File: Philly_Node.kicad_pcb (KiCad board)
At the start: 2 copper layers, 22 x 38.8 mm, 50 parts, among them J4 USB_C_Receptacle_USB2.0, J5 J-Link, Q4 Q_NMOS_GSD, U1 MDBT50Q-U1MV2, U2 BQ25101, U7 E22-900M22S, Y1 32.768KHz

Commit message: Nearly done, final part number checks needed.
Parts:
- removed D6, D7, D8: LESD5D5_0CT1G, pager_parts:SOD-523_L1.2-W0.8-LS1.6-BI
- added C7: 100uf, Capacitor_SMD:CP_Elec_5x4.5, B.Cu at (97.7, 50.0)
- added F1: Polyfuse 3.5A, Fuse:Fuse_1206_3216Metric, F.Cu at (99.0, 58.6)
- added J1: LED, Connector_PinSocket_1.00mm:PinSocket_1x03_P1.00mm_Vertical, F.Cu at (98.4, 75.7)
- added Q1: Q_Dual_NMOS_G1S2G2D2S1D1, Library:DFN-6-1EP_2x2mm_P0.65mm_EP_DUAL, B.Cu at (81.9, 76.5)
- added R22: 22, Resistor_SMD:R_0402_1005Metric, B.Cu at (87.2, 77.2)
- added R23: 1M, Resistor_SMD:R_0402_1005Metric, B.Cu at (85.2, 77.2)
- added R24: 22, Resistor_SMD:R_0402_1005Metric, B.Cu at (87.2, 76.2)
- added R25: 1M, Resistor_SMD:R_0402_1005Metric, B.Cu at (85.2, 76.2)
- added SOL1: S2B-PH-SM4-TB, Connector_JST:JST_PH_S2B-PH-SM4-TB_1x02-1MP_P2.00mm_Horizontal, F.Cu at (85.8, 50.0)
- D1, D2: value 1N5819WS -> B5819WT; footprint Diode_SMD:D_SOD-323 -> Diode_SMD:D_SOD-523
- J5: value J-Link -> Multi
- moved D3 4.70 mm to (99.3, 62.7)
- moved D2 3.17 mm to (90.2, 46.6), turned to 90 degrees
- moved R11 2.29 mm to (100.8, 76.2), turned to -90 degrees
- moved R16 2.13 mm to (97.8, 64.4)
- moved R6 1.43 mm to (90.9, 54.6)
- moved LED1 1.40 mm to (98.3, 79.0)
- moved R10 1.19 mm to (99.8, 76.2), turned to -90 degrees
- moved D1 1.14 mm to (90.8, 53.1)
- moved R5 0.92 mm to (85.7, 55.5)
- moved D5 0.66 mm to (81.2, 56.3)
- moved D4 0.63 mm to (82.7, 56.3)
- moved BAT1 0.62 mm to (96.6, 51.2)
- moved Q4 0.30 mm to (99.4, 66.2), turned to 180 degrees
- renumbered BT1 to BAT1
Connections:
- BAT1 pad 1: /VBAT -> /VBAT_UNFUSED
- C30 pad 1: /VBAT -> /VBAT_UNFUSED
- D3 pad 2: /VBAT -> /VBAT_FUSED
- J5 pad 10: unconnected-(J5-Pin_10-Pad10) -> NMOS_2
- J5 pad 5: GND -> P1.12_RX
- J5 pad 6: unconnected-(J5-Pin_6-Pad6) -> P1.11_TX
- J5 pad 7: unconnected-(J5-Pin_7-Pad7) -> GND
- J5 pad 8: unconnected-(J5-Pin_8-Pad8) -> VBAT_POL_PROT
- J5 pad 9: GND -> NMOS_1
- R8 pad 1: /VBAT -> /VBAT_UNFUSED
- U1 pad 4: unconnected-(U1-P1.11-Pad4) -> P1.11_TX
- U1 pad 42: unconnected-(U1-P0.19-Pad42) -> P0.19
- U1 pad 44: unconnected-(U1-P0.20-Pad44) -> P0.20
- U1 pad 5: unconnected-(U1-P1.12-Pad5) -> P1.12_RX
- U2 pad A1: /VBAT -> /VBAT_UNFUSED
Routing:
- net /VBAT_UNFUSED: track 0.00 -> 39.9 mm, vias 0 -> 2
- net /VBAT: track 36.1 -> 0.00 mm, vias 2 -> 0
- net GND: track 41.3 -> 65.9 mm, vias 26 -> 29
- net P1.11_TX: track 0.00 -> 24.3 mm, vias 0 -> 1
- net P1.12_RX: track 0.00 -> 24.0 mm, vias 0 -> 1
- net VBAT_POL_PROT: track 62.4 -> 80.0 mm
- net NMOS_1: track 0.00 -> 8.49 mm
- net P0.19: track 0.00 -> 8.28 mm, vias 0 -> 1
- net NMOS_2: track 0.00 -> 7.55 mm
- net P0.20: track 0.00 -> 6.62 mm, vias 0 -> 1
- net Net-(Q1B-G): track 0.00 -> 6.41 mm, vias 0 -> 2
- net Net-(Q1A-G): track 0.00 -> 5.50 mm
- net P0.30_USER_GREEN: track 7.36 -> 11.8 mm, vias 2 -> 1
- net P0.26_USER_RED: track 12.3 -> 15.3 mm, vias 2 -> 1
- net Net-(LED1-B-): track 6.29 -> 9.09 mm
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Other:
- board text added: "B G R"
- board text added: "MICRO NODE"
- board text added: "O19­↓"
- board text added: "O20→"
- board text added: "V+"
- board text added: "V1.0"
- board text added: "_GND"
- board text added: "_RX"
- board text added: "_TX"
- board text removed: "MICRO NODE V1.0"

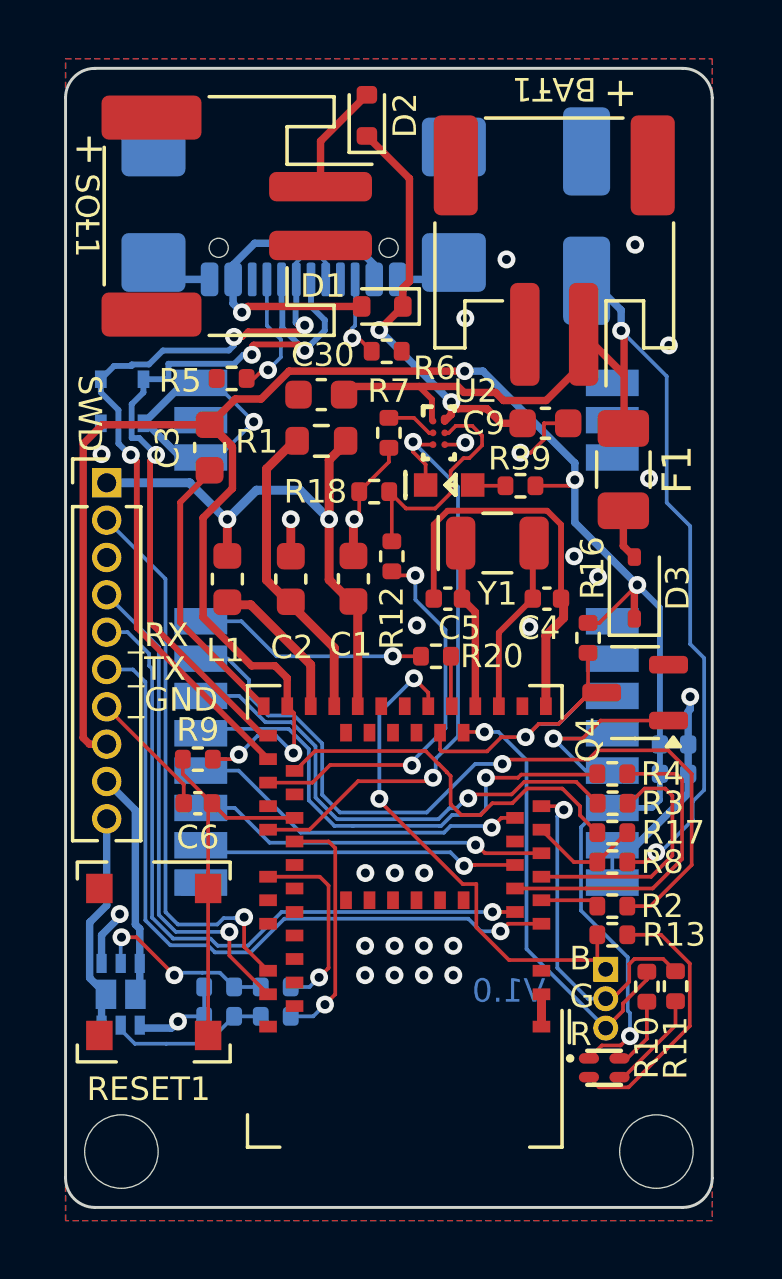
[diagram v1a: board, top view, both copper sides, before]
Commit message: Added D0 button, NFC pads, and library files.
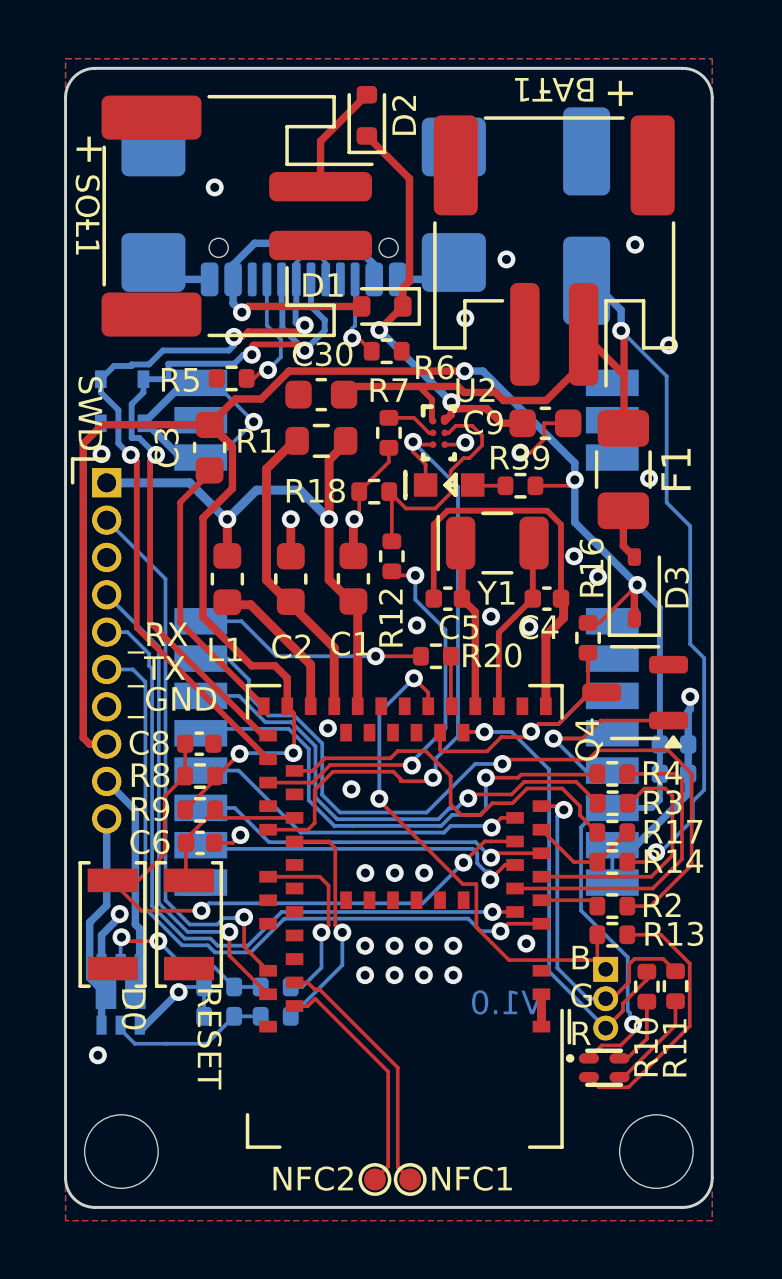
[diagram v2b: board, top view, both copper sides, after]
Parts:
- added C8: 0.1uF, Philly_Lib:C_0402_1005Metric, F.Cu at (84.5, 68.0)
- added NFC1: TestPoint, Philly_Lib:TestPoint_Pad_D0.75mm, F.Cu at (91.7, 82.8)
- added NFC2: TestPoint, Philly_Lib:TestPoint_Pad_D0.75mm, F.Cu at (90.5, 82.8)
- added R8: 10k, Philly_Lib:R_0402_1005Metric, F.Cu at (84.6, 69.1)
- added SW2: D0, Philly_Lib:SW_Tactile_SPST_NO_Straight_TVAF44-N015C-R, F.Cu at (81.6, 74.1)
- BAT1: footprint Library:JST_PH_S2B-PH-SM4-TB_1x02-1MP_P2.00mm_Horizontal_GND -> Philly_Lib:JST_PH_S2B-PH-SM4-TB_1x02-1MP_P2.00mm_Horizontal_GND
- C1, C2, C3, C30, C9: footprint Capacitor_SMD:C_0603_1608Metric -> Philly_Lib:C_0603_1608Metric
- C12, C13, C4, C5: footprint Capacitor_SMD:C_0402_1005Metric -> Philly_Lib:C_0402_1005Metric
- C6: value 100nF -> 0.1uF; footprint Capacitor_SMD:C_0402_1005Metric -> Philly_Lib:C_0402_1005Metric
- C7: footprint Capacitor_SMD:CP_Elec_5x4.5 -> Philly_Lib:CP_Elec_5x4.5
- D1, D2: footprint Diode_SMD:D_SOD-523 -> Philly_Lib:D_SOD-523
- D3: footprint Diode_SMD:D_SOD-323 -> Philly_Lib:D_SOD-323
- D4, D5: footprint pager_parts:SOD-523_L1.2-W0.8-LS1.6-BI -> Philly_Lib:SOD-523_L1.2-W0.8-LS1.6-BI
- F1: footprint Fuse:Fuse_1206_3216Metric -> Philly_Lib:Fuse_1206_3216Metric
- H1, H2: footprint MountingHole:MountingHole_2.5mm -> Philly_Lib:MountingHole_2.5mm
- J1: footprint Connector_PinSocket_1.00mm:PinSocket_1x03_P1.00mm_Vertical -> Philly_Lib:PinSocket_1x03_P1.00mm_Vertical
- J4: footprint Library:USB_C_Receptacle_GCT_USB4110_MODIFIED_FOR_PROTRSION -> Philly_Lib:USB_C_Receptacle_GCT_USB4110_MODIFIED_FOR_PROTRSION
- J5: footprint Connector_PinHeader_1.27mm:PinHeader_1x10_P1.27mm_Vertical -> Philly_Lib:PinHeader_1x10_P1.27mm_Vertical
- L1: footprint Inductor_SMD:L_0603_1608Metric -> Philly_Lib:L_0603_1608Metric
- LED1: footprint pager_parts:LED-ARRAY-SMD_4P-L1.0-W1.0-TR-RD -> Philly_Lib:LED-ARRAY-SMD_4P-L1.0-W1.0-TR-RD
- LED57: footprint pager_parts:LED0603-RD -> Philly_Lib:LED0603-RD
- Q1: footprint Library:DFN-6-1EP_2x2mm_P0.65mm_EP_DUAL -> Philly_Lib:DFN-6-1EP_2x2mm_P0.65mm_EP_DUAL
- Q4: footprint Package_TO_SOT_SMD:SOT-23-3 -> Philly_Lib:SOT-23-3
- R1: footprint Resistor_SMD:R_0603_1608Metric -> Philly_Lib:R_0603_1608Metric
- R10, R11, R12, R13, R16, R18, R2, R20, R22, R23, R24, R25, R3, R39, R4, R5, R6, R7, R9: footprint Resistor_SMD:R_0402_1005Metric -> Philly_Lib:R_0402_1005Metric
- R14: renamed from R8; value 1M_1% -> 1M; footprint Resistor_SMD:R_0402_1005Metric -> Philly_Lib:R_0402_1005Metric
- R17: value 510k_1% -> 510k; footprint Resistor_SMD:R_0402_1005Metric -> Philly_Lib:R_0402_1005Metric
- RESET1: footprint Library:TS1187A26015 -> Philly_Lib:SW_Tactile_SPST_NO_Straight_TVAF44-N015C-R
- SOL1: footprint Connector_JST:JST_PH_S2B-PH-SM4-TB_1x02-1MP_P2.00mm_Horizontal -> Philly_Lib:JST_PH_S2B-PH-SM4-TB_1x02-1MP_P2.00mm_Horizontal
- U1: footprint RF_Module:Raytac_MDBT50Q -> Philly_Lib:Raytac_MDBT50Q
- U2: footprint Philly_Node_Lib:YFP0006AFAV -> Philly_Lib:YFP0006AFAV
- U7: footprint pager_parts:WIRELM-SMD_E22-900M22S -> Philly_Lib:WIRELM-SMD_E22-900M22S
- Y1: footprint Crystal:Crystal_SMD_MicroCrystal_CC7V-T1A-2Pin_3.2x1.5mm -> Philly_Lib:Crystal_SMD_MicroCrystal_CC7V-T1A-2Pin_3.2x1.5mm
- moved RESET1 1.75 mm to (84.2, 74.1)
- moved R9 1.73 mm to (84.6, 70.2), turned to 180 degrees
- moved C6 1.35 mm to (84.6, 71.3), turned to 0 degrees
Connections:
- BAT1 pad GND: (no net) -> GND
- U1 pad 11: unconnected-(U1-P0.02/AIN0-Pad11) -> D0
- U1 pad 52: unconnected-(U1-P0.09/NFC1-Pad52) -> /NFC+
- U1 pad 54: unconnected-(U1-P0.10/NFC2-Pad54) -> /NFC-
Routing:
- net D0: track 0.00 -> 21.4 mm, vias 0 -> 2
- net /NFC+: track 0.00 -> 8.69 mm
- net /NFC-: track 0.00 -> 8.32 mm
- net Net-(U1-~{RESET}/P0.18): track 13.4 -> 5.71 mm
- net GND: track 65.9 -> 63.1 mm, vias 29 -> 36
- net VBAT_POL_PROT: track 80.0 -> 81.4 mm
- net P0.17_~{CHG}: track 21.1 -> 22.1 mm
- net LORA_DIO1: track 11.0 -> 11.7 mm
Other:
- board text added: "RESET D0"

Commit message: Added courtyards, updated schematic to point to local lib footprints.
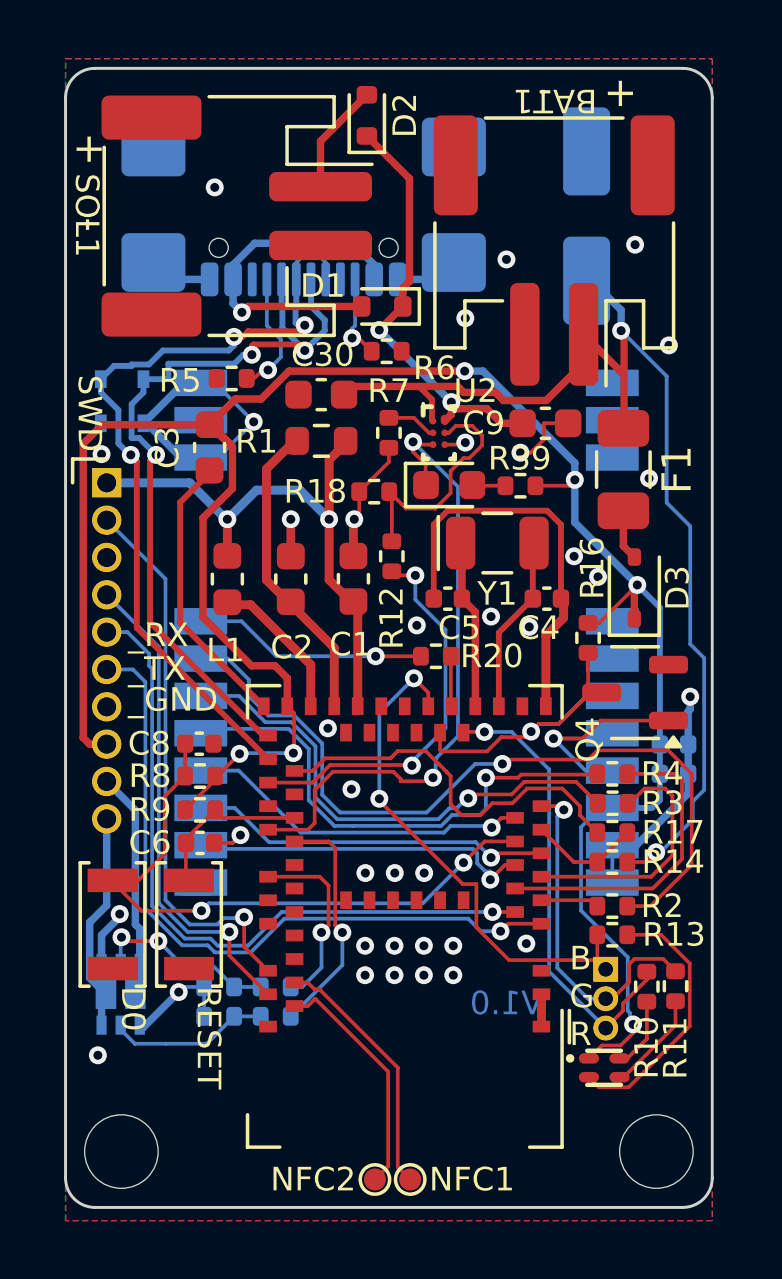
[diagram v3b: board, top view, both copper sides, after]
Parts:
- BAT1: footprint Philly_Lib:JST_PH_S2B-PH-SM4-TB_1x02-1MP_P2.00mm_Horizontal_GND -> Philly_Lib:JST_PH_S2B-PH-SM4-TB_1x02-1MP_P2.00mm_Horizontal
- LED57: footprint Philly_Lib:LED0603-RD -> Philly_Lib:LED_0603_1608Metric

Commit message: changed to BQ25176JDSGR charge IC
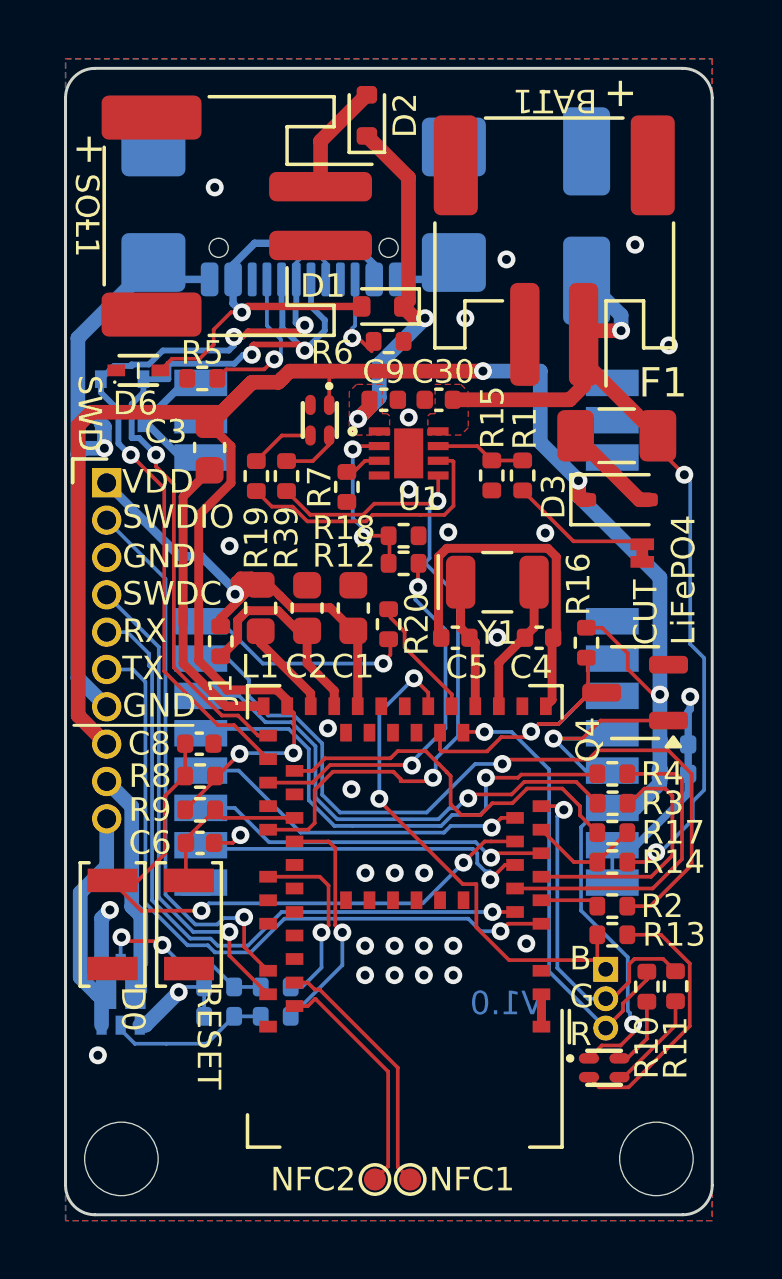
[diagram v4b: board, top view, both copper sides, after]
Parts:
- removed LED57: KT-0603R, Philly_Lib:LED_0603_1608Metric
- removed the U2 at (92.7, 57.4)
- added D6: LESD5D5_0CT1G, Philly_Lib:SOD-523_L1.2-W0.8-LS1.6-BI, F.Cu at (82.5, 55.3)
- added JP2: LiFePO4, Philly_Lib:SolderJumper, F.Cu at (99.6, 61.5)
- added LED2: MHPA1010RGBDT, Philly_Lib:LED-ARRAY-SMD_4P-L1.0-W1.0-TR-RD, F.Cu at (88.7, 57.0)
- added R1: 34.8k, Philly_Lib:R_0402_1005Metric, F.Cu at (95.5, 58.9)
- added R15: 82.5k, Philly_Lib:R_0402_1005Metric, F.Cu at (94.5, 58.9)
- added R19: 10K, Philly_Lib:R_0402_1005Metric, F.Cu at (86.5, 58.9)
- added U1: BQ25176JDSGR, Philly_Lib:WSON_MDSGR_TEX, F.Cu at (91.7, 58.1)
- BAT1: value Battery_Cell -> S2B-PH-SM4-TB
- C30, C9: footprint Philly_Lib:C_0603_1608Metric -> Philly_Lib:C_0402_1005Metric
- J1: renamed from R1; footprint Philly_Lib:R_0603_1608Metric -> Philly_Lib:R_0402_1005Metric
- R12: value 2.7k -> 510
- R18: value 2.7k -> 1.5k
- moved R39 7.96 mm to (87.5, 58.9), turned to 90 degrees
- moved J1 7.63 mm to (85.3, 64.5), turned to -90 degrees
- moved C9 5.56 mm to (90.8, 56.3)
- moved C30 4.00 mm to (92.7, 56.3)
- moved D3 3.05 mm to (98.8, 59.7), turned to 0 degrees
- moved R7 2.33 mm to (89.6, 59.2)
- moved R20 1.94 mm to (91.0, 63.9), turned to -90 degrees
- moved R18 1.80 mm to (91.5, 60.9), turned to 0 degrees
- moved L1 1.50 mm to (86.6, 63.4)
- moved C4 1.36 mm to (96.1, 64.4)
- moved C5 1.35 mm to (93.3, 64.4)
- moved Y1 1.33 mm to (94.7, 62.5)
- moved F1 1.17 mm to (98.8, 57.5), turned to 180 degrees
- moved C2 1.13 mm to (88.2, 63.4)
- moved R5 1.00 mm to (84.7, 55.5)
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- renumbered J1 to J2, U1 to U2, U7 to U3
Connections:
- C12 pad 1: VBAT_POL_PROT -> /VBAT_POL_PROT
- C13 pad 1: VBAT_POL_PROT -> /VBAT_POL_PROT
- C3 pad 2: VBAT_POL_PROT -> /VBAT_POL_PROT
- D3 pad 1: VBAT_POL_PROT -> /VBAT_POL_PROT
- J5 pad 8: VBAT_POL_PROT -> /VBAT_POL_PROT
- LED1 pad 1: VBAT_POL_PROT -> /VBAT_POL_PROT
- R16 pad 1: VBAT_POL_PROT -> /VBAT_POL_PROT
- R39 pad 1: VBAT_POL_PROT -> P0.17_~{CHG}
- R8 pad 2: VBAT_POL_PROT -> /VBAT_POL_PROT
- R9 pad 2: VBAT_POL_PROT -> /VBAT_POL_PROT
- U2 pad 32: VBAT_POL_PROT -> /VBAT_POL_PROT
- U3 pad 9: VBAT_POL_PROT -> /VBAT_POL_PROT
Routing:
- net /VBAT_POL_PROT: track 0.00 -> 83.3 mm, vias 0 -> 6
- net VBAT_POL_PROT: track 81.4 -> 0.00 mm, vias 6 -> 0
- net ~{PG}: track 0.00 -> 9.39 mm
- net GND: track 63.1 -> 71.2 mm, vias 36 -> 31
- net /VBAT_UNFUSED: track 39.9 -> 32.3 mm, vias 2 -> 3
- net Net-(JP2-B): track 0.00 -> 4.84 mm
- net /VBUS: track 11.8 -> 15.9 mm
- net Net-(U1-VSET): track 0.00 -> 3.11 mm
- net /VDD: track 19.8 -> 16.7 mm, vias 2 -> 1
- net Net-(U2-VDDH): track 10.4 -> 7.49 mm
- net P0.17_~{CHG}: track 22.1 -> 24.3 mm
- net LORA_NSS: track 1.71 -> 3.93 mm
- net Net-(LED2-G-): track 0.00 -> 2.20 mm
- net Net-(D1-K): track 14.6 -> 12.6 mm
- net Net-(U1-ISET): track 8.16 -> 6.13 mm, vias 0 -> 2
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- added copper zone on F.Cu, net /VBAT_UNFUSED
- added copper zone on F.Cu, net Net-(D1-K)
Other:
- board size 22 x 38.8 mm -> 22 x 39 mm
- board text added: "CUT LiFePO4"
- board text added: "GND"
- board text added: "RX"
- board text added: "SWDC"
- board text added: "SWDIO"
- board text added: "TX"
- board text added: "VDD"
- board text removed: "_GND"
- board text removed: "_RX"
- board text removed: "_TX"
